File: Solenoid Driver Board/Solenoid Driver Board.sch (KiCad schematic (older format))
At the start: 25 parts, among them J1 CH1, J2 Solenoid, J3 RGB_LED, J4 DEBUG, J5 MAIN, J6 CH2, J7 CH3, J8 MAIN, Q1 IRLB8721PBF, U1 AMS1117-5.0, U2 STM8S003F3P

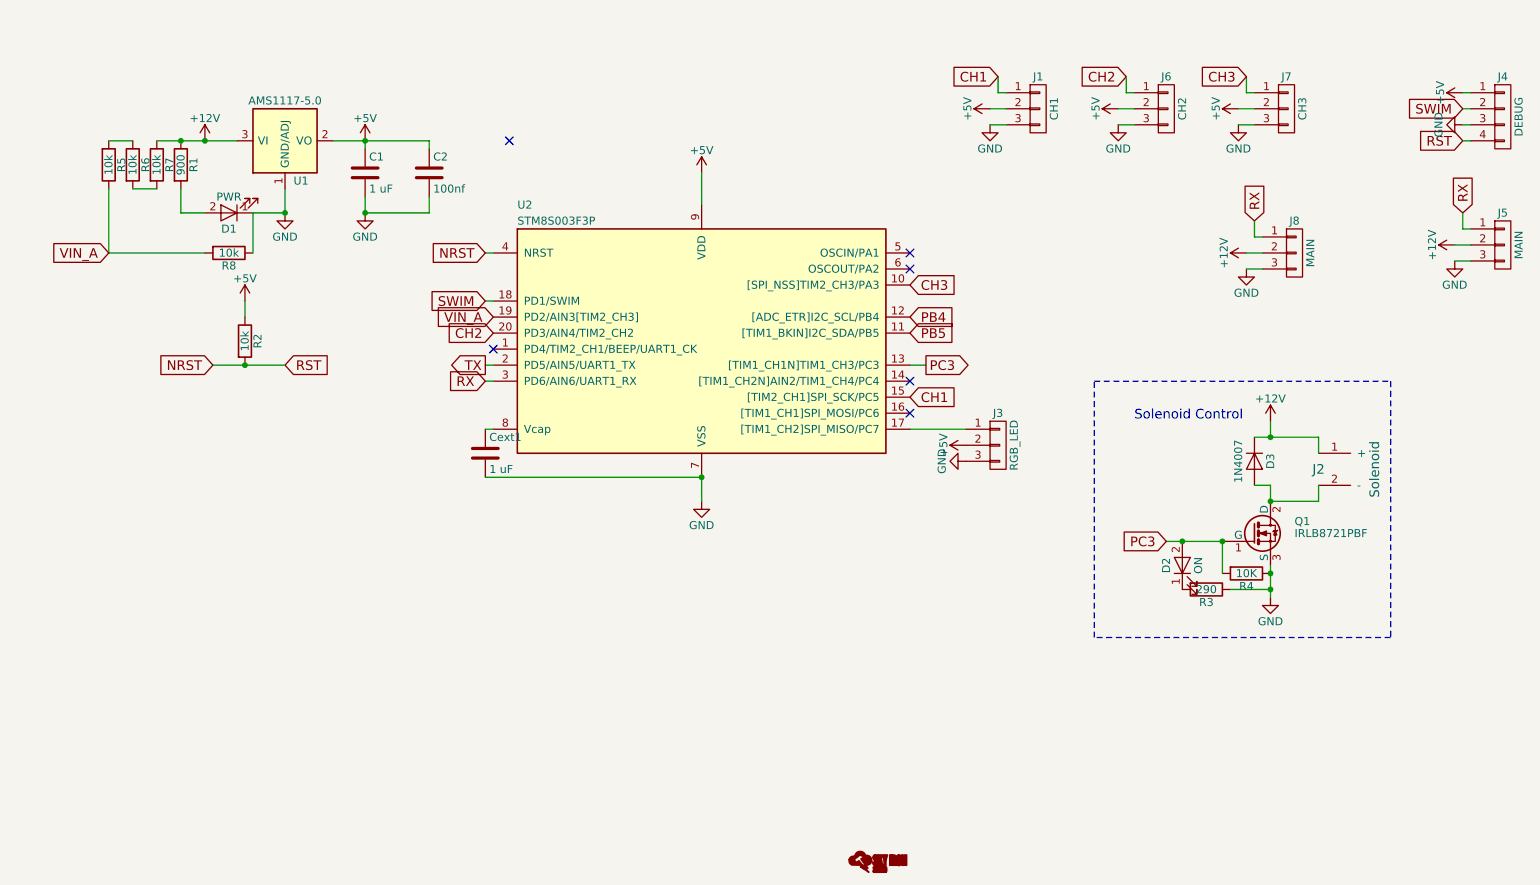
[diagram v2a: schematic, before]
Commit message: Added IWDG timer support
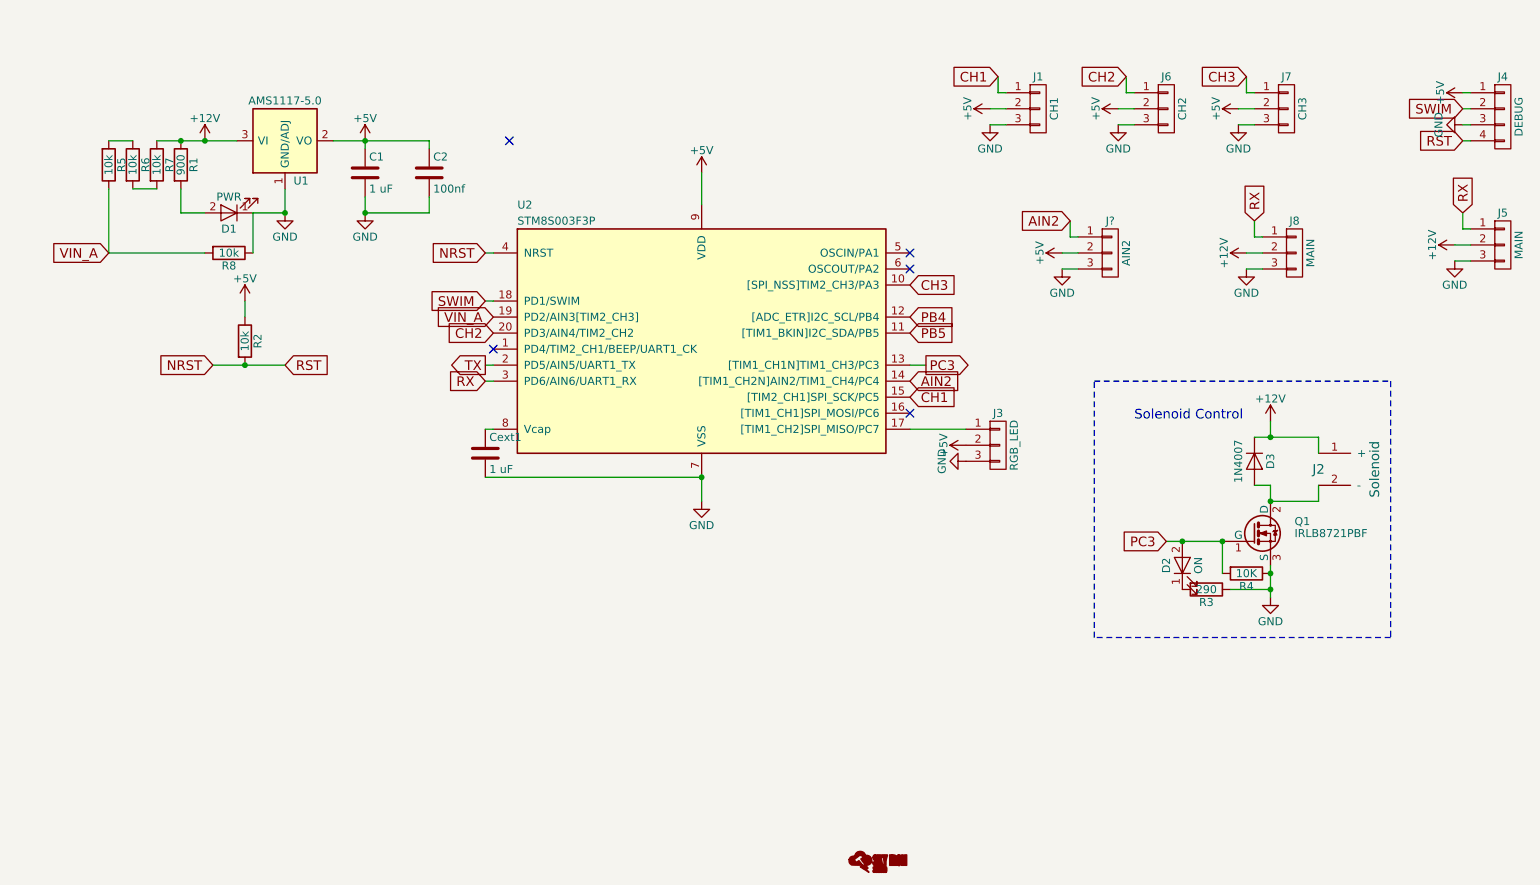
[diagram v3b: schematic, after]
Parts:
- added J?: AIN2, Pin_Headers:Pin_Header_Straight_1x03_Pitch2.54mm, symbol CONN_01X03
- R5, R6, R7, R8: footprint Resistors_SMD:R_0805_HandSoldering -> Resistors_SMD:R_1206_HandSoldering
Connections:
- net +5V: now also J?.2 (P2)
- net GND: now also J?.3 (P3)
- net AIN2: now reaches U2.14 ([TIM1_CH2N]AIN2/TIM1_CH4/PC4)
- net AIN2: now also J?.1 (P1)
- no-connect marks 6 -> 5
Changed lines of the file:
@@
 $EndComp
 $Comp
-L +12V #PWR1
+L +12V #PWR01
 U 1 1 58F576B7
 P 2100 1400
-F 0 "#PWR1" H 2100 1250 50  0001 C CNN
+F 0 "#PWR01" H 2100 1250 50  0001 C CNN
 F 1 "+12V" H 2100 1540 50  0000 C CNN
 F 2 "" H 2100 1400 50  0001 C CNN
@@
 $EndComp
 $Comp
-L +5V #PWR4
+L +5V #PWR02
 U 1 1 58F576D3
 P 3100 1400
-F 0 "#PWR4" H 3100 1250 50  0001 C CNN
+F 0 "#PWR02" H 3100 1250 50  0001 C CNN
 F 1 "+5V" H 3100 1540 50  0000 C CNN
 F 2 "" H 3100 1400 50  0001 C CNN
@@
 $EndComp
 $Comp
-L GND #PWR3
+L GND #PWR03
 U 1 1 58F576F3
 P 2600 1850
-F 0 "#PWR3" H 2600 1600 50  0001 C CNN
+F 0 "#PWR03" H 2600 1600 50  0001 C CNN
 F 1 "GND" H 2600 1700 50  0000 C CNN
 F 2 "" H 2600 1850 50  0001 C CNN
@@
 	2600 1850 2600 1700
 Wire Wire Line
-	2900 1400 3500 1400
-$Comp
-L +5V #PWR6
+	2900 1400 3100 1400
+Wire Wire Line
+	3100 1400 3500 1400
+$Comp
+L +5V #PWR04
 U 1 1 58F5771C
 P 5200 1600
-F 0 "#PWR6" H 5200 1450 50  0001 C CNN
+F 0 "#PWR04" H 5200 1450 50  0001 C CNN
 F 1 "+5V" H 5200 1740 50  0000 C CNN
 F 2 "" H 5200 1600 50  0001 C CNN
@@
 $EndComp
 $Comp
-L GND #PWR7
+L GND #PWR05
 U 1 1 58F57736
 P 5200 3650
-F 0 "#PWR7" H 5200 3400 50  0001 C CNN
+F 0 "#PWR05" H 5200 3400 50  0001 C CNN
 F 1 "GND" H 5200 3500 50  0000 C CNN
 F 2 "" H 5200 3650 50  0001 C CNN
@@
 SWIM
 $Comp
-L GND #PWR23
+L GND #PWR06
 U 1 1 58F57AF4
 P 9950 1300
-F 0 "#PWR23" H 9950 1050 50  0001 C CNN
+F 0 "#PWR06" H 9950 1050 50  0001 C CNN
 F 1 "GND" H 9950 1150 50  0000 C CNN
 F 2 "" H 9950 1300 50  0001 C CNN
@@
 $EndComp
 $Comp
-L +5V #PWR22
+L +5V #PWR07
 U 1 1 58F57B17
 P 9950 1100
-F 0 "#PWR22" H 9950 950 50  0001 C CNN
+F 0 "#PWR07" H 9950 950 50  0001 C CNN
 F 1 "+5V" H 9950 1240 50  0000 C CNN
 F 2 "" H 9950 1100 50  0001 C CNN
@@
 $EndComp
 $Comp
-L GND #PWR19
+L GND #PWR08
 U 1 1 58F58125
 P 8750 4250
-F 0 "#PWR19" H 8750 4000 50  0001 C CNN
+F 0 "#PWR08" H 8750 4000 50  0001 C CNN
 F 1 "GND" H 8750 4100 50  0000 C CNN
 F 2 "" H 8750 4250 50  0001 C CNN
@@
 PC3
 Wire Wire Line
-	8100 3900 8450 3900
+	8100 3900 8200 3900
+Wire Wire Line
+	8200 3900 8450 3900
 Wire Wire Line
 	8450 3900 8450 4100
 Wire Wire Line
-	8750 4050 8750 4250
+	8750 4050 8750 4100
+Wire Wire Line
+	8750 4100 8750 4200
+Wire Wire Line
+	8750 4200 8750 4250
 Connection ~ 8750 4100
 $Comp
@@
 $EndComp
 $Comp
-L +12V #PWR18
+L +12V #PWR09
 U 1 1 58F5833A
 P 8750 3150
-F 0 "#PWR18" H 8750 3000 50  0001 C CNN
+F 0 "#PWR09" H 8750 3000 50  0001 C CNN
 F 1 "+12V" H 8750 3290 50  0000 C CNN
 F 2 "" H 8750 3150 50  0001 C CNN
@@
 $EndComp
 $Comp
-L +12V #PWR20
+L +12V #PWR010
 U 1 1 58F586EE
 P 9900 2050
-F 0 "#PWR20" H 9900 1900 50  0001 C CNN
+F 0 "#PWR010" H 9900 1900 50  0001 C CNN
 F 1 "+12V" H 9900 2190 50  0000 C CNN
 F 2 "" H 9900 2050 50  0001 C CNN
@@
 $EndComp
 $Comp
-L GND #PWR21
+L GND #PWR011
 U 1 1 58F58726
 P 9900 2150
-F 0 "#PWR21" H 9900 1900 50  0001 C CNN
+F 0 "#PWR011" H 9900 1900 50  0001 C CNN
 F 1 "GND" H 9900 2000 50  0000 C CNN
 F 2 "" H 9900 2150 50  0001 C CNN
@@
 	3850 2800 3900 2800
 Wire Wire Line
-	8650 3250 9050 3250
+	8650 3250 8750 3250
+Wire Wire Line
+	8750 3250 9050 3250
 Wire Wire Line
 	8750 3250 8750 3150
@@
 $EndComp
 $Comp
-L +5V #PWR2
+L +5V #PWR012
 U 1 1 58FB95C2
 P 2350 2400
-F 0 "#PWR2" H 2350 2250 50  0001 C CNN
+F 0 "#PWR012" H 2350 2250 50  0001 C CNN
 F 1 "+5V" H 2350 2540 50  0000 C CNN
 F 2 "" H 2350 2400 50  0001 C CNN
@@
 	2350 2400 2350 2500
 Wire Wire Line
-	2150 2800 2600 2800
+	2150 2800 2350 2800
+Wire Wire Line
+	2350 2800 2600 2800
 Text GLabel 2150 2800 0    60   Input ~ 0
 NRST
@@
 RST
 Wire Wire Line
-	1800 1400 2300 1400
+	1800 1400 1950 1400
+Wire Wire Line
+	1950 1400 2100 1400
+Wire Wire Line
+	2100 1400 2300 1400
 Connection ~ 2100 1400
 $Comp
-L GND #PWR5
+L GND #PWR013
 U 1 1 58FBA70F
 P 3100 1850
-F 0 "#PWR5" H 3100 1600 50  0001 C CNN
+F 0 "#PWR013" H 3100 1600 50  0001 C CNN
 F 1 "GND" H 3100 1700 50  0000 C CNN
 F 2 "" H 3100 1850 50  0001 C CNN
@@
 	6500 3200 6850 3200
 $Comp
-L +5V #PWR8
+L +5V #PWR014
 U 1 1 5904B931
 P 6850 3300
-F 0 "#PWR8" H 6850 3150 50  0001 C CNN
+F 0 "#PWR014" H 6850 3150 50  0001 C CNN
 F 1 "+5V" H 6850 3440 50  0000 C CNN
 F 2 "" H 6850 3300 50  0001 C CNN
@@
 $EndComp
 $Comp
-L GND #PWR9
+L GND #PWR015
 U 1 1 5904B984
 P 6850 3400
-F 0 "#PWR9" H 6850 3150 50  0001 C CNN
+F 0 "#PWR015" H 6850 3150 50  0001 C CNN
 F 1 "GND" H 6850 3250 50  0000 C CNN
 F 2 "" H 6850 3400 50  0001 C CNN
@@
 F 0 "R7" V 1880 1550 50  0000 C CNN
 F 1 "10k" V 1800 1550 50  0000 C CNN
-F 2 "Resistors_SMD:R_0805_HandSoldering" V 1730 1550 50  0001 C CNN
+F 2 "Resistors_SMD:R_1206_HandSoldering" V 1730 1550 50  0001 C CNN
 F 3 "" H 1800 1550 50  0001 C CNN
 	1    1800 1550
@@
 F 0 "R6" V 1730 1550 50  0000 C CNN
 F 1 "10k" V 1650 1550 50  0000 C CNN
-F 2 "Resistors_SMD:R_0805_HandSoldering" V 1580 1550 50  0001 C CNN
+F 2 "Resistors_SMD:R_1206_HandSoldering" V 1580 1550 50  0001 C CNN
 F 3 "" H 1650 1550 50  0001 C CNN
 	1    1650 1550
@@
 F 0 "R5" V 1580 1550 50  0000 C CNN
 F 1 "10k" V 1500 1550 50  0000 C CNN
-F 2 "Resistors_SMD:R_0805_HandSoldering" V 1430 1550 50  0001 C CNN
+F 2 "Resistors_SMD:R_1206_HandSoldering" V 1430 1550 50  0001 C CNN
 F 3 "" H 1500 1550 50  0001 C CNN
 	1    1500 1550
@@
 F 0 "R8" V 2330 2100 50  0000 C CNN
 F 1 "10k" V 2250 2100 50  0000 C CNN
-F 2 "Resistors_SMD:R_0805_HandSoldering" V 2180 2100 50  0001 C CNN
+F 2 "Resistors_SMD:R_1206_HandSoldering" V 2180 2100 50  0001 C CNN
 F 3 "" H 2250 2100 50  0001 C CNN
 	1    2250 2100
@@
 $EndComp
 $Comp
-L +12V #PWR16
+L +12V #PWR016
 U 1 1 594F0627
 P 8600 2100
-F 0 "#PWR16" H 8600 1950 50  0001 C CNN
+F 0 "#PWR016" H 8600 1950 50  0001 C CNN
 F 1 "+12V" H 8600 2240 50  0000 C CNN
 F 2 "" H 8600 2100 50  0001 C CNN
@@
 $EndComp
 $Comp
-L GND #PWR17
+L GND #PWR017
 U 1 1 594F062D
 P 8600 2200
-F 0 "#PWR17" H 8600 1950 50  0001 C CNN
+F 0 "#PWR017" H 8600 1950 50  0001 C CNN
 F 1 "GND" H 8600 2050 50  0000 C CNN
 F 2 "" H 8600 2200 50  0001 C CNN
@@
 $EndComp
 $Comp
-L GND #PWR11
+L GND #PWR018
 U 1 1 594F0877
 P 7000 1300
-F 0 "#PWR11" H 7000 1050 50  0001 C CNN
+F 0 "#PWR018" H 7000 1050 50  0001 C CNN
 F 1 "GND" H 7000 1150 50  0000 C CNN
 F 2 "" H 7000 1300 50  0001 C CNN
@@
 	7050 1100 7100 1100
 $Comp
-L +5V #PWR10
+L +5V #PWR019
 U 1 1 594F0C76
 P 7000 1200
-F 0 "#PWR10" H 7000 1050 50  0001 C CNN
+F 0 "#PWR019" H 7000 1050 50  0001 C CNN
 F 1 "+5V" H 7000 1340 50  0000 C CNN
 F 2 "" H 7000 1200 50  0001 C CNN
@@
 $EndComp
 $Comp
-L GND #PWR13
+L GND #PWR020
 U 1 1 594F0D4C
 P 7800 1300
-F 0 "#PWR13" H 7800 1050 50  0001 C CNN
+F 0 "#PWR020" H 7800 1050 50  0001 C CNN
 F 1 "GND" H 7800 1150 50  0000 C CNN
 F 2 "" H 7800 1300 50  0001 C CNN
@@
 	7850 1100 7900 1100
 $Comp
-L +5V #PWR12
+L +5V #PWR021
 U 1 1 594F0D57
 P 7800 1200
-F 0 "#PWR12" H 7800 1050 50  0001 C CNN
+F 0 "#PWR021" H 7800 1050 50  0001 C CNN
 F 1 "+5V" H 7800 1340 50  0000 C CNN
 F 2 "" H 7800 1200 50  0001 C CNN
@@
 $EndComp
 $Comp
-L GND #PWR15
+L GND #PWR022
 U 1 1 594F0E91
 P 8550 1300
-F 0 "#PWR15" H 8550 1050 50  0001 C CNN
+F 0 "#PWR022" H 8550 1050 50  0001 C CNN
 F 1 "GND" H 8550 1150 50  0000 C CNN
 F 2 "" H 8550 1300 50  0001 C CNN
@@
 	8600 1100 8650 1100
 $Comp
-L +5V #PWR14
+L +5V #PWR023
 U 1 1 594F0E9C
 P 8550 1200
-F 0 "#PWR14" H 8550 1050 50  0001 C CNN
+F 0 "#PWR023" H 8550 1050 50  0001 C CNN
 F 1 "+5V" H 8550 1340 50  0000 C CNN
 F 2 "" H 8550 1200 50  0001 C CNN
@@
 NoConn ~ 6500 2100
 NoConn ~ 6500 2200
-NoConn ~ 6500 2900
 NoConn ~ 6500 3100
+Text GLabel 6500 2900 2    60   Input ~ 0
+AIN2
+$Comp
+L CONN_01X03 J?
+U 1 1 594FC604
+P 7750 2100
+F 0 "J?" H 7750 2300 50  0000 C CNN
+F 1 "AIN2" V 7850 2100 50  0000 C CNN
+F 2 "Pin_Headers:Pin_Header_Straight_1x03_Pitch2.54mm" H 7750 2100 50  0001 C CNN
+F 3 "" H 7750 2100 50  0001 C CNN
+	1    7750 2100
+	1    0    0    -1
+$EndComp
+$Comp
+L GND #PWR?
+U 1 1 594FC60A
+P 7450 2200
+F 0 "#PWR?" H 7450 1950 50  0001 C CNN
+F 1 "GND" H 7450 2050 50  0000 C CNN
+F 2 "" H 7450 2200 50  0001 C CNN
+F 3 "" H 7450 2200 50  0001 C CNN
+	1    7450 2200
+	1    0    0    -1
+$EndComp
+Text GLabel 7500 1900 0    60   Input ~ 0
+AIN2
+Wire Wire Line
+	7500 1900 7500 2000
+Wire Wire Line
+	7450 2100 7550 2100
+Wire Wire Line
+	7450 2200 7550 2200
+Wire Wire Line
+	7500 2000 7550 2000
+$Comp
+L +5V #PWR?
+U 1 1 594FC615
+P 7450 2100
+F 0 "#PWR?" H 7450 1950 50  0001 C CNN
+F 1 "+5V" H 7450 2240 50  0000 C CNN
+F 2 "" H 7450 2100 50  0001 C CNN
+F 3 "" H 7450 2100 50  0001 C CNN
+	1    7450 2100
+	0    -1   -1   0
+$EndComp
 $EndSCHEMATC

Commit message: Layout work begun on v1.1 of PCB
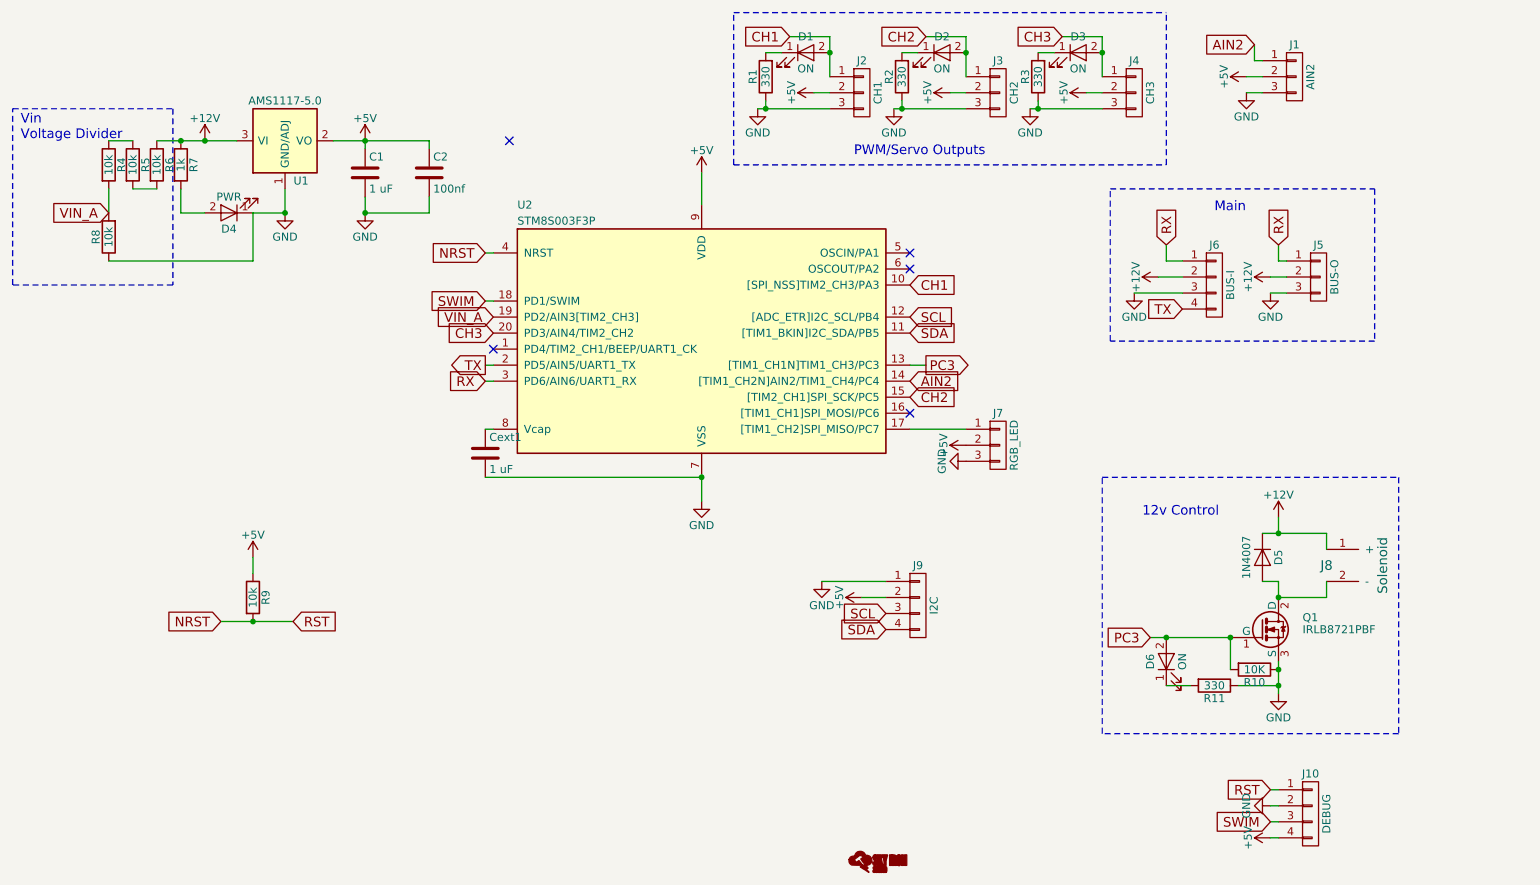
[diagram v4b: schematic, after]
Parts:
- removed J6: CH2, Pin_Headers:Pin_Header_Straight_1x03_Pitch2.54mm, symbol CONN_01X03
- removed J7: CH3, Pin_Headers:Pin_Header_Straight_1x03_Pitch2.54mm, symbol CONN_01X03
- removed J8: MAIN, Pin_Headers:Pin_Header_Straight_1x03_Pitch2.54mm, symbol CONN_01X03
- added D1, D2, D3: ON, SpadeConnector:LED_0805_Bottom_Hole, symbol LED
- added J3: CH2, Pin_Headers:Pin_Header_Straight_1x03_Pitch2.54mm, symbol CONN_01X03
- added J4: CH3, Pin_Headers:Pin_Header_Straight_1x03_Pitch2.54mm, symbol CONN_01X03
- added J6: BUS-I, Pin_Headers:Pin_Header_Straight_1x04_Pitch2.54mm, symbol CONN_01X04
- added J9: I2C, Pin_Headers:Pin_Header_Straight_1x04_Pitch2.54mm, symbol CONN_01X04
- added R1, R2, R3: 330, Resistors_SMD:R_0805_HandSoldering, symbol R
- D4: renamed from D1; footprint LEDs:LED_0805 -> SpadeConnector:LED_0805_Bottom_Hole
- D6: renamed from D2; footprint LEDs:LED_0805 -> SpadeConnector:LED_0805_Bottom_Hole
- J5: value MAIN -> BUS-O
- R11: renamed from R3; value 290 -> 330
- R7: renamed from R1; value 900 -> 1k
- gave numbers to parts that had none: 1
- renumbered D3 to D5, J4 to J10, J1 to J2, J3 to J7, J2 to J8, R4 to R10, R5 to R4, R6 to R5, R7 to R6, R2 to R9
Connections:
- net +12V: now also J6.2 (P2)
- net +5V: now also J10.4 (P4), J3.2 (P2), J4.2 (P2), J9.2 (P2); no longer J10.1 (P1)
- net CH1: now also U2.10 ([SPI_NSS]TIM2_CH3/PA3), D1.2 (A); no longer U2.15 ([TIM2_CH1]SPI_SCK/PC5)
- net CH2: now also U2.15 ([TIM2_CH1]SPI_SCK/PC5), D2.2 (A), J3.1 (P1); no longer U2.20 (PD3/AIN4/TIM2_CH2)
- net CH3: now also U2.20 (PD3/AIN4/TIM2_CH2), D3.2 (A), J4.1 (P1); no longer U2.10 ([SPI_NSS]TIM2_CH3/PA3)
- net GND: now also J10.2 (P2), J3.3 (P3), J4.3 (P3), J6.3 (P3), J9.1 (P1), R1.1, R2.1, R3.1; no longer J10.3 (P3)
- net NRST: now also J10.1 (P1); no longer J10.4 (P4)
- net RX: now also J6.1 (P1)
- net SWIM: now also J10.3 (P3); no longer J10.2 (P2)
- net TX: now also J6.4 (P4)
- net VIN_A: now also R4.2; no longer R4.1
- net at R5.1: now also R4.1; no longer R4.2
- net PB4 renamed SCL
- net SCL: now also J9.3 (P3)
- net PB5 renamed SDA
- net SDA: now also J9.4 (P4)
- new net: D1.1 (K), R1.2
- new net: D2.1 (K), R2.2
- new net: D3.1 (K), R3.2
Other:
- note added: "12v Control"
- note added: "Main"
- note added: "PWM/Servo Outputs"
- note added: "Vin \nVoltage Divider"
- note removed: "Solenoid Control"
- moved on the sheet: D5, D6, J1, J10, J2, J5, J8, Q1, R10, R11, R8, R9

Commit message: New source image
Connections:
- net CH3 is gone; now on net CH2: D3.2 (A), J4.1 (P1), U2.20 (PD3/AIN4/TIM2_CH2)
- net CH1: now also D2.2 (A), J3.1 (P1), U2.15 ([TIM2_CH1]SPI_SCK/PC5); no longer D1.2 (A), J2.1 (P1), U2.10 ([SPI_NSS]TIM2_CH3/PA3)
- net CH2: no longer D2.2 (A), J3.1 (P1), U2.15 ([TIM2_CH1]SPI_SCK/PC5)
- new net CH0: D1.2 (A), J2.1 (P1), U2.10 ([SPI_NSS]TIM2_CH3/PA3)
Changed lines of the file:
@@
 $EndComp
 Text GLabel 6500 2300 2    60   Input ~ 0
+CH0
+Text GLabel 3900 2600 0    60   Input ~ 0
+CH2
+Text GLabel 6500 3000 2    60   Input ~ 0
 CH1
-Text GLabel 3900 2600 0    60   Input ~ 0
-CH3
-Text GLabel 6500 3000 2    60   Input ~ 0
-CH2
 $Comp
 L R R6
@@
 $EndComp
 Text GLabel 5750 750  0    60   Input ~ 0
-CH1
+CH0
 Wire Wire Line
 	5900 1100 6000 1100
@@
 $EndComp
 Text GLabel 6600 750  0    60   Input ~ 0
-CH2
+CH1
 Wire Wire Line
 	6750 1100 6850 1100
@@
 $EndComp
 Text GLabel 7450 750  0    60   Input ~ 0
-CH3
+CH2
 Wire Wire Line
 	7600 1100 7700 1100
